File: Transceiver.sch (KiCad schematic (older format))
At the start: 28 parts

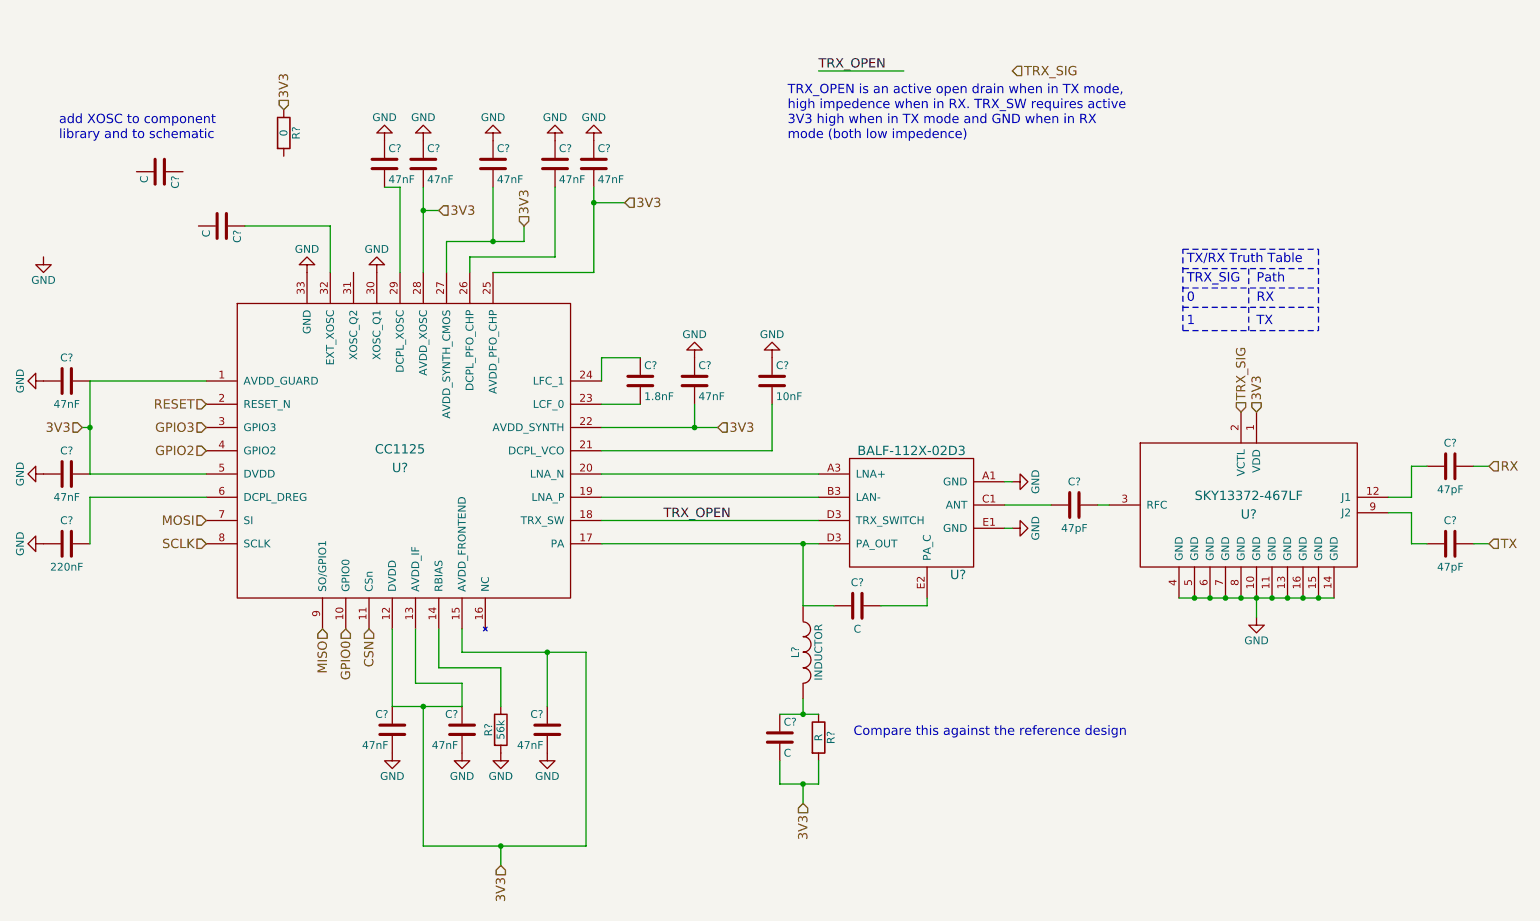
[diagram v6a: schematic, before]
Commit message: Added XOSC
-Changed the VDD pin of the RF switch to a power input
-Added the XOSC (symbol and footprint)
-Made some modifications to the transceiver page
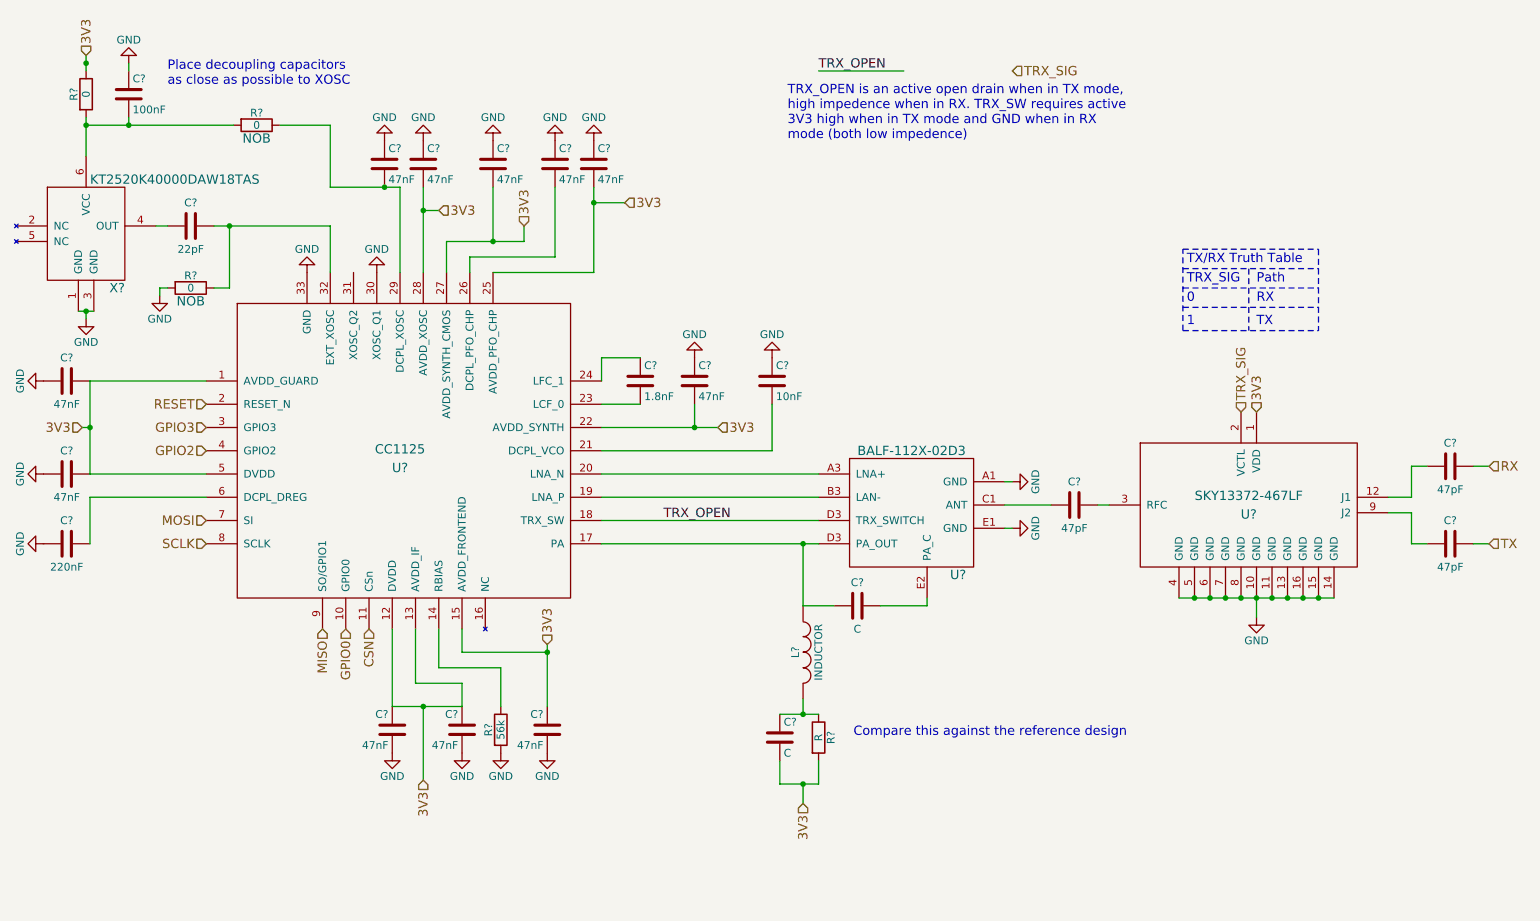
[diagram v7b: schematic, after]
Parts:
- added R? (x2): 0, symbol R
- added X?: KT2520K40000DAW18TAS, symbol KT2520K40000DAW18TAS
- C?: value C -> 22pF
- C?: value C -> 100nF
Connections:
- net GND: now also C?.1, R?.2, X?.1 (GND), X?.3 (GND)
- net at C?.2, U?.29 (DCPL_XOSC): now also R?.1
- net at C?.1, U?.32 (EXT_XOSC): now also R?.1
- net at C?.2: now also X?.4 (OUT)
- net at R?.2: now also C?.2, R?.2, X?.6 (VCC)
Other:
- note added: "Place decoupling capacitors\nas close as possible to XOSC\n"
- note removed: "add XOSC to component \nlibrary and to schematic\n"
- moved on the sheet: C?, R?
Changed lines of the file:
@@
 L C C?
 U 1 1 5821C9DD
-P 1900 2000
-F 0 "C?" H 1925 2100 50  0000 L CNN
-F 1 "C" H 1925 1900 50  0000 L CNN
-F 2 "" H 1938 1850 50  0000 C CNN
-F 3 "" H 1900 2000 50  0000 C CNN
-	1    1900 2000
+P 1700 2000
+F 0 "C?" V 1550 2000 50  0000 C CNN
+F 1 "22pF" V 1850 2000 50  0000 C CNN
+F 2 "" H 1738 1850 50  0000 C CNN
+F 3 "" H 1700 2000 50  0000 C CNN
+	1    1700 2000
 	0    1    1    0
 $EndComp
@@
 L R R?
 U 1 1 5821C9EC
-P 2300 1400
-F 0 "R?" V 2380 1400 50  0000 C CNN
-F 1 "0" V 2300 1400 50  0000 C CNN
-F 2 "" V 2230 1400 50  0000 C CNN
-F 3 "" H 2300 1400 50  0000 C CNN
-	1    2300 1400
+P 1025 1150
+F 0 "R?" V 975 1150 50  0000 C BNN
+F 1 "0" V 1025 1150 50  0000 C CNN
+F 2 "" V 955 1150 50  0000 C CNN
+F 3 "" H 1025 1150 50  0000 C CNN
+	1    1025 1150
 	1    0    0    -1
 $EndComp
@@
 L C C?
 U 1 1 5821C9F3
-P 1500 1650
-F 0 "C?" H 1525 1750 50  0000 L CNN
-F 1 "C" H 1525 1550 50  0000 L CNN
-F 2 "" H 1538 1500 50  0000 C CNN
-F 3 "" H 1500 1650 50  0000 C CNN
-	1    1500 1650
-	0    1    1    0
+P 1300 1150
+F 0 "C?" H 1325 1250 50  0000 L CNN
+F 1 "100nF" H 1325 1050 50  0000 L CNN
+F 2 "" H 1338 1000 50  0000 C CNN
+F 3 "" H 1300 1150 50  0000 C CNN
+	1    1300 1150
+	1    0    0    -1
 $EndComp
 $Comp
 L GND #PWR018
 U 1 1 5821C9FA
-P 750 2200
-F 0 "#PWR018" H 750 1950 50  0001 C CNN
-F 1 "GND" H 750 2050 50  0000 C CNN
-F 2 "" H 750 2200 50  0000 C CNN
-F 3 "" H 750 2200 50  0000 C CNN
-	1    750  2200
+P 1025 2600
+F 0 "#PWR018" H 1025 2350 50  0001 C CNN
+F 1 "GND" H 1025 2450 50  0000 C CNN
+F 2 "" H 1025 2600 50  0000 C CNN
+F 3 "" H 1025 2600 50  0000 C CNN
+	1    1025 2600
 	1    0    0    -1
 $EndComp
@@
 Text HLabel 1000 3300 0    60   Input ~ 0
 3V3
-Text HLabel 2300 1250 1    60   Input ~ 0
+Text HLabel 1025 900  1    60   Input ~ 0
 3V3
 Text HLabel 3300 1900 2    60   Input ~ 0
@@
 	0    -1   -1   0
 $EndComp
-Text HLabel 3700 6125 3    60   Input ~ 0
+Text HLabel 3200 5575 3    60   Input ~ 0
 3V3
 Text HLabel 5100 3300 2    60   Input ~ 0
@@
 Text Notes 5550 1450 0    60   ~ 0
 TRX_OPEN is an active open drain when in TX mode, \nhigh impedence when in RX. TRX_SW requires active \n3V3 high when in TX mode and GND when in RX \nmode (both low impedence)
-Text Notes 850  1450 0    60   ~ 0
-add XOSC to component \nlibrary and to schematic\n
+Text Notes 1550 1100 0    60   ~ 0
+Place decoupling capacitors\nas close as possible to XOSC\n
 Text HLabel 8575 3200 1    60   Input ~ 0
 3V3
@@
 Connection ~ 3200 1900
 Wire Wire Line
-	3050 2300 3050 1750
-Wire Wire Line
-	3050 1750 2950 1750
-Wire Wire Line
-	3000 4600 3000 5100
-Wire Wire Line
-	3000 5100 3450 5100
+	3050 1750 3050 2300
+Wire Wire Line
+	2600 1750 3050 1750
 Wire Wire Line
 	3450 5100 3450 4950
@@
 Wire Wire Line
 	3450 4600 3450 4750
-Wire Wire Line
-	3450 4750 4250 4750
-Wire Wire Line
-	4000 4750 4000 5100
-Wire Wire Line
-	4250 4750 4250 6000
 Connection ~ 4000 4750
 Wire Wire Line
@@
 	4350 4050 5750 4050
 Wire Wire Line
-	2600 2300 2600 2000
-Wire Wire Line
-	2600 2000 2050 2000
+	2600 2000 2600 2300
 Wire Wire Line
 	5500 5150 5750 5150
@@
 	5650 4050 5650 4450
 Connection ~ 5650 4050
-Wire Wire Line
-	4250 6000 3200 6000
-Wire Wire Line
-	3200 6000 3200 5100
 Connection ~ 3200 5100
 Wire Wire Line
@@
 Connection ~ 5650 5600
 Wire Wire Line
-	3700 6125 3700 6000
-Connection ~ 3700 6000
+	3200 5100 3200 5575
 Text Notes 5975 5300 0    60   ~ 0
 Compare this against the reference design
+$Comp
+L KT2520K40000DAW18TAS X?
+U 1 1 58734E44
+P 1025 2050
+F 0 "X?" H 1175 1700 60  0000 L CNN
+F 1 "KT2520K40000DAW18TAS" H 1050 2400 60  0000 L CNN
+F 2 "" H 1725 2300 60  0001 C CNN
+F 3 "" H 1725 2300 60  0001 C CNN
+	1    1025 2050
+	1    0    0    -1
+$EndComp
+Wire Wire Line
+	975  2550 1075 2550
+Connection ~ 1025 2550
+Wire Wire Line
+	1025 2550 1025 2600
+Wire Wire Line
+	1850 2000 2600 2000
+Wire Wire Line
+	1025 1000 1025 900
+Wire Wire Line
+	1025 1300 1025 1550
+Connection ~ 1025 950
+Wire Wire Line
+	1300 1300 1300 1350
+$Comp
+L GND #PWR?
+U 1 1 5873A98A
+P 1300 950
+F 0 "#PWR?" H 1300 700 50  0001 C CNN
+F 1 "GND" H 1300 800 50  0000 C CNN
+F 2 "" H 1300 950 50  0000 C CNN
+F 3 "" H 1300 950 50  0000 C CNN
+	1    1300 950
+	-1   0    0    1
+$EndComp
+Wire Wire Line
+	1025 1350 1975 1350
+Connection ~ 1025 1350
+Wire Wire Line
+	1300 1000 1300 950
+$Comp
+L R R?
+U 1 1 5873B49B
+P 2125 1350
+F 0 "R?" V 2075 1350 50  0000 C BNN
+F 1 "0" V 2125 1350 50  0000 C CNN
+F 2 "" V 2055 1350 50  0000 C CNN
+F 3 "" H 2125 1350 50  0000 C CNN
+F 4 "NOB" V 2175 1350 60  0000 C TNN "Populated"
+	1    2125 1350
+	0    1    1    0
+$EndComp
+Connection ~ 1300 1350
+Wire Wire Line
+	2275 1350 2600 1350
+Wire Wire Line
+	2600 1350 2600 1750
+Connection ~ 2950 1750
+Wire Wire Line
+	1475 2000 1550 2000
+$Comp
+L R R?
+U 1 1 5873DE02
+P 1700 2400
+F 0 "R?" V 1650 2400 50  0000 C BNN
+F 1 "0" V 1700 2400 50  0000 C CNN
+F 2 "" V 1630 2400 50  0000 C CNN
+F 3 "" H 1700 2400 50  0000 C CNN
+F 4 "NOB" V 1750 2400 60  0000 C TNN "Populated"
+	1    1700 2400
+	0    1    1    0
+$EndComp
+Wire Wire Line
+	1950 2000 1950 2400
+Wire Wire Line
+	1950 2400 1850 2400
+Connection ~ 1950 2000
+Wire Wire Line
+	1550 2400 1500 2400
+Wire Wire Line
+	1500 2400 1500 2450
+$Comp
+L GND #PWR?
+U 1 1 5873E01A
+P 1500 2450
+F 0 "#PWR?" H 1500 2200 50  0001 C CNN
+F 1 "GND" H 1500 2300 50  0000 C CNN
+F 2 "" H 1500 2450 50  0000 C CNN
+F 3 "" H 1500 2450 50  0000 C CNN
+	1    1500 2450
+	1    0    0    -1
+$EndComp
+Wire Wire Line
+	3000 5100 3450 5100
+Wire Wire Line
+	3000 5100 3000 4600
+Wire Wire Line
+	3450 4750 4000 4750
+Text HLabel 4000 4700 1    60   Input ~ 0
+3V3
+Wire Wire Line
+	4000 4700 4000 5100
 $EndSCHEMATC

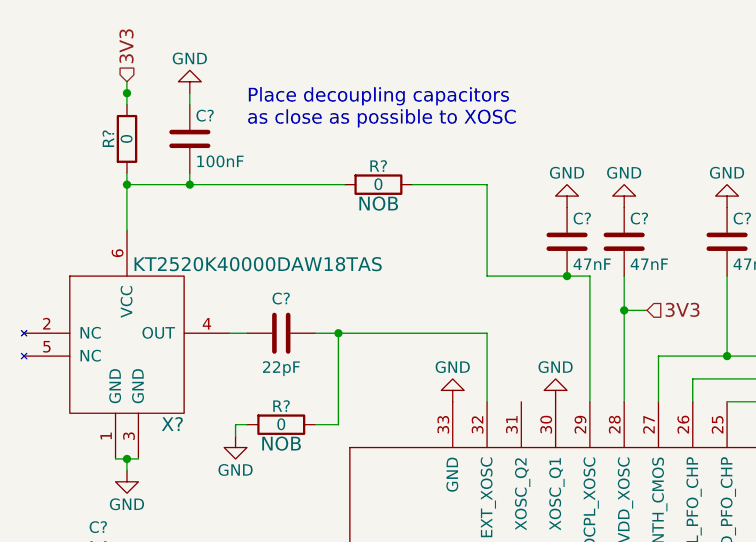
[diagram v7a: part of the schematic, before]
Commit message: Fixed XOSC
-Changed 3V3 rail of XOSC to 1V8 as specified in datasheet
-Changed XOSC capacitor values to match the datasheet
-Added 1V8 rail to SFUSat-Radio.sch Transceiver and Power pages
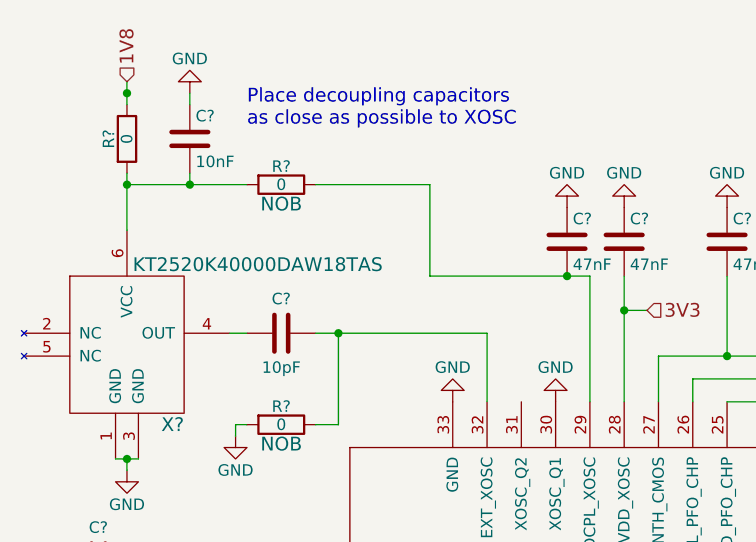
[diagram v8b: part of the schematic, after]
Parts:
- removed R?: 0, symbol R
- added R?: 0, symbol R
- C?: value 22pF -> 10pF
- C?: value 100nF -> 10nF
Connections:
- net 3V3: no longer R?.1
- net at C?.2, U?.29 (DCPL_XOSC): now also R?.1
- net at C?.2, R?.2, X?.6 (VCC): now also R?.2
- new net 1V8: R?.1
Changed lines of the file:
@@
 P 1700 2000
 F 0 "C?" V 1550 2000 50  0000 C CNN
-F 1 "22pF" V 1850 2000 50  0000 C CNN
+F 1 "10pF" V 1850 2000 50  0000 C CNN
 F 2 "" H 1738 1850 50  0000 C CNN
 F 3 "" H 1700 2000 50  0000 C CNN
@@
 P 1300 1150
 F 0 "C?" H 1325 1250 50  0000 L CNN
-F 1 "100nF" H 1325 1050 50  0000 L CNN
+F 1 "10nF" H 1325 1050 50  0000 L CNN
 F 2 "" H 1338 1000 50  0000 C CNN
 F 3 "" H 1300 1150 50  0000 C CNN
@@
 3V3
 Text HLabel 1025 900  1    60   Input ~ 0
-3V3
+1V8
 Text HLabel 3300 1900 2    60   Input ~ 0
 3V3
@@
 	3050 1750 3050 2300
 Wire Wire Line
-	2600 1750 3050 1750
-Wire Wire Line
 	3450 5100 3450 4950
 Wire Wire Line
@@
 	-1   0    0    1
 $EndComp
-Wire Wire Line
-	1025 1350 1975 1350
 Connection ~ 1025 1350
 Wire Wire Line
 	1300 1000 1300 950
-$Comp
-L R R?
-U 1 1 5873B49B
-P 2125 1350
-F 0 "R?" V 2075 1350 50  0000 C BNN
-F 1 "0" V 2125 1350 50  0000 C CNN
-F 2 "" V 2055 1350 50  0000 C CNN
-F 3 "" H 2125 1350 50  0000 C CNN
-F 4 "NOB" V 2175 1350 60  0000 C TNN "Populated"
-	1    2125 1350
-	0    1    1    0
-$EndComp
-Connection ~ 1300 1350
-Wire Wire Line
-	2275 1350 2600 1350
-Wire Wire Line
-	2600 1350 2600 1750
 Connection ~ 2950 1750
 Wire Wire Line
@@
 Wire Wire Line
 	4000 4700 4000 5100
+Wire Wire Line
+	1025 1350 1550 1350
+Wire Wire Line
+	2350 1750 3050 1750
+$Comp
+L R R?
+U 1 1 58748BE0
+P 1700 1350
+F 0 "R?" V 1650 1350 50  0000 C BNN
+F 1 "0" V 1700 1350 50  0000 C CNN
+F 2 "" V 1630 1350 50  0000 C CNN
+F 3 "" H 1700 1350 50  0000 C CNN
+F 4 "NOB" V 1750 1350 60  0000 C TNN "Populated"
+	1    1700 1350
+	0    1    1    0
+$EndComp
+Connection ~ 1300 1350
+Wire Wire Line
+	2350 1750 2350 1350
+Wire Wire Line
+	2350 1350 1850 1350
 $EndSCHEMATC
